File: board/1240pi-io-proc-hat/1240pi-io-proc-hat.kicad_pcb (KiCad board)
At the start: 2 copper layers, 29.2 x 58.4 mm, 7 parts, among them J21 Header, P445 Header, U445 Z80

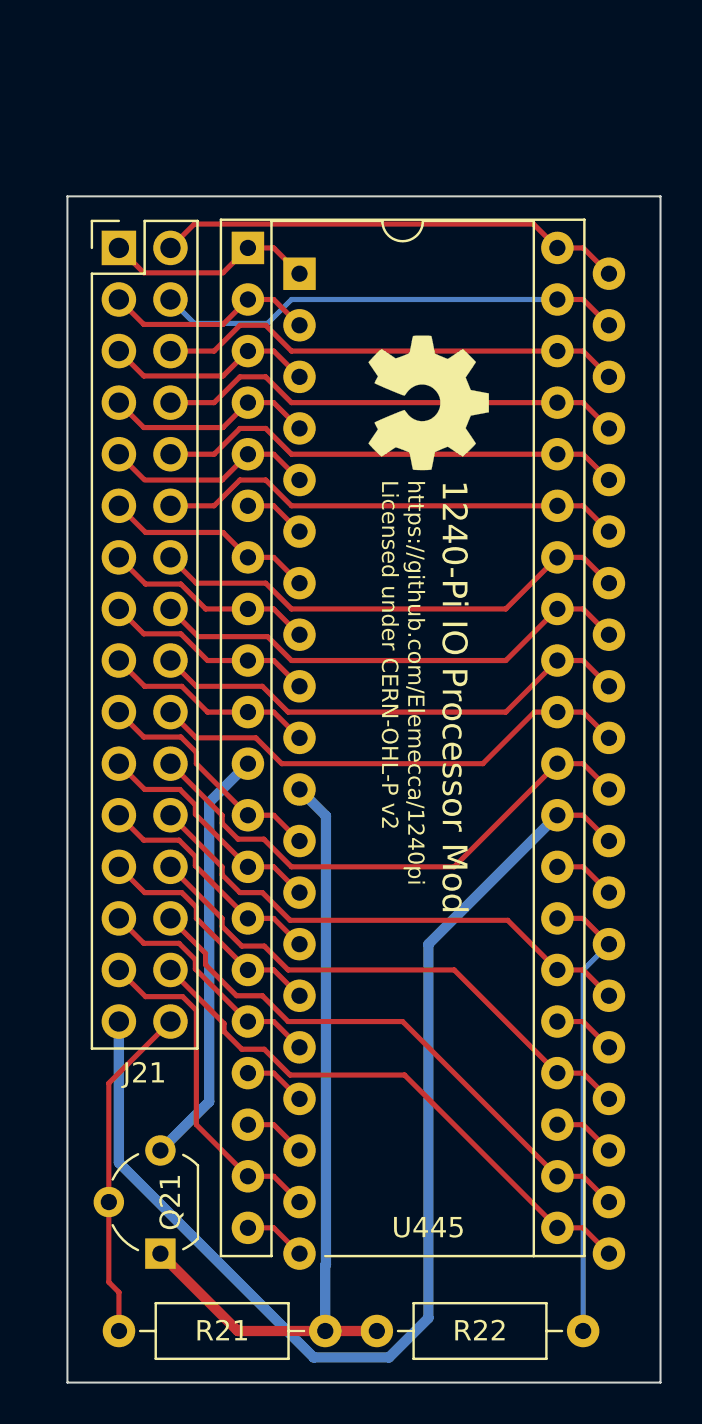
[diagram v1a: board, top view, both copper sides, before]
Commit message: Switch hat boards from IDC ribbons to flat flex cables.
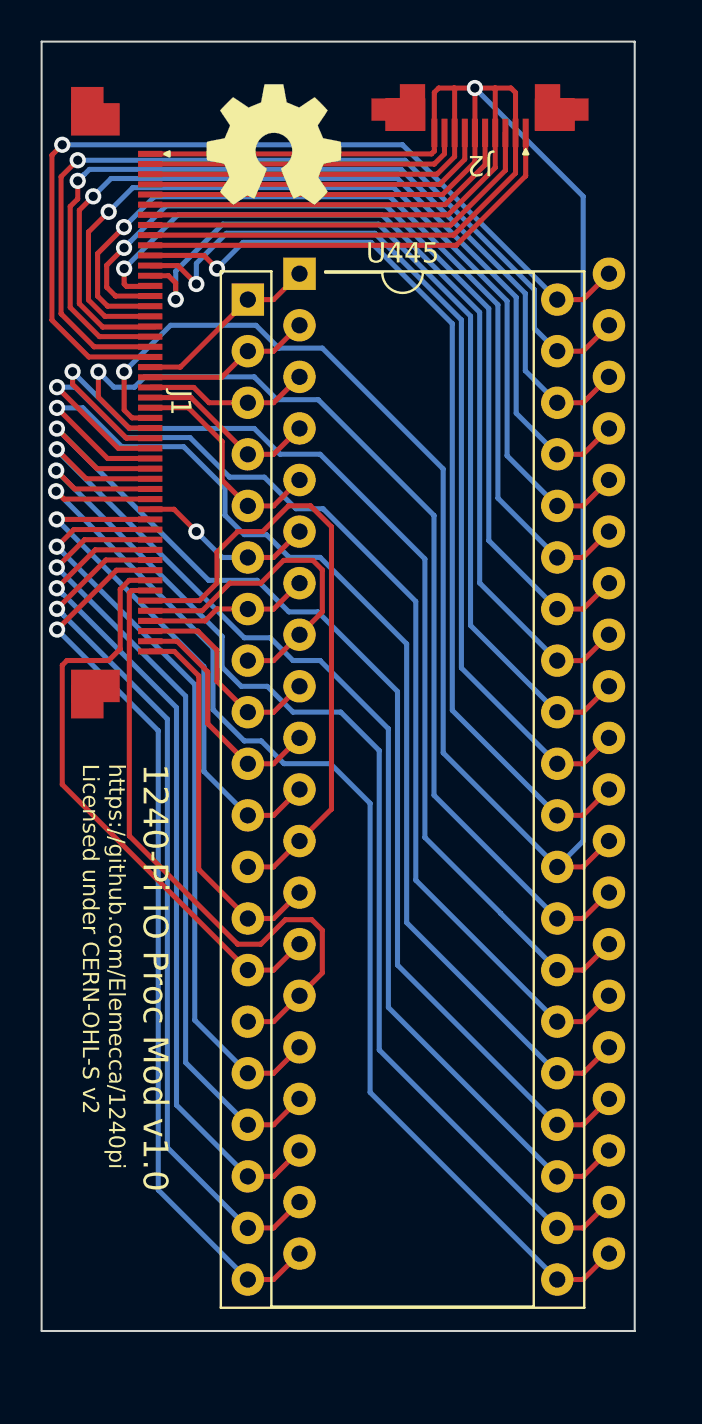
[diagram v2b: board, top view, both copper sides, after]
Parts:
- removed J21: Header, Connector_PinHeader_2.54mm:PinHeader_2x16_P2.54mm_Vertical
- removed Q21: ~, Package_TO_SOT_THT:TO-92_Wide
- removed R21, R22: 10k, Resistor_THT:R_Axial_DIN0207_L6.3mm_D2.5mm_P10.16mm_Horizontal
- added J1: 62684-50210, 0Local:Amphenol_62684-50210, F.Cu at (137.7, 58.4)
- added J2: SFV10R-1ST, 0Local:Amphenol_SFV10R-1ST, F.Cu at (156.2, 43.4)
- moved REF** 14.8 mm to (146.1, 45.7), turned to 0 degrees
- moved U445 2.55 mm to (144.8, 53.3)
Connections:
- U445 pad 11: Net-(Q21-Pad3) -> +5V
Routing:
- net GND: track 57.4 -> 194.3 mm, vias 0 -> 2
- net /~{BUSACK}: track 3.07 -> 55.8 mm, vias 0 -> 1
- net /~{BUSRQ}: track 3.07 -> 55.7 mm, vias 0 -> 1
- net /~{RFSH}: track 3.07 -> 49.8 mm, vias 0 -> 1
- net /~{IORQ}: track 3.07 -> 44.8 mm, vias 0 -> 1
- net /~{HALT}: track 3.07 -> 41.3 mm, vias 0 -> 1
- net /~{NMI}: track 3.07 -> 39.6 mm, vias 0 -> 1
- net /~{RD}: track 27.6 -> 58.7 mm, vias 0 -> 1
- net /~{M1}: track 22.6 -> 52.7 mm, vias 0 -> 1
- net /~{WR}: track 27.7 -> 57.7 mm, vias 0 -> 1
- net /~{RESET}: track 25.5 -> 54.5 mm, vias 0 -> 1
- net /~{WAIT}: track 26.6 -> 55.2 mm, vias 0 -> 1
- net /~{MREQ}: track 16.9 -> 43.0 mm, vias 0 -> 1
- net /~{INT}: track 11.8 -> 37.9 mm, vias 0 -> 1
- net /~{EXT_EN}: track 0.00 -> 22.0 mm
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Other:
- board size 29.2 x 58.4 mm -> 29.2 x 63.5 mm
- board text added: "1240-Pi IO Proc Mod v${REVISION}"
- board text added: "https://github.com/Elemecca/1240pi Licensed under CERN-OHL-S v2"
- board text removed: "1240-Pi IO Processor Mod"
- board text removed: "https://github.com/Elemecca/1240pi Licensed under CERN-OHL-P v2"

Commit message: Update board license to CERN-OHL-S v2+.
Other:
- board text added: "https://github.com/Elemecca/1240pi Licensed under CERN-OHL-S v2+"
- board text removed: "https://github.com/Elemecca/1240pi Licensed under CERN-OHL-S v2"
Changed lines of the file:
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@@
     (date "2022-05-21")
     (rev "1.0")
-    (company "© 2022 Sam Hanes, licensed under CERN-OHL-S v2")
+    (company "© 2022 Sam Hanes, licensed under CERN-OHL-S v2+")
     (comment 1 "https://github.com/Elemecca/1240pi")
-    (comment 4 "AISLER Project ID: UZHORLNP")
   )
   (layers
@@
     (effects (font (size 1.2192 1.2192) (thickness 0.2032)) (justify left))
   )
-  (gr_text "https://github.com/Elemecca/1240pi\nLicensed under CERN-OHL-S v2" (at 137.668 76.2 -90) (layer "F.SilkS")
+  (gr_text "https://github.com/Elemecca/1240pi\nLicensed under CERN-OHL-S v2+" (at 137.668 76.2 -90) (layer "F.SilkS")
     (effects (font (size 0.8 0.8) (thickness 0.1)) (justify left))
   )

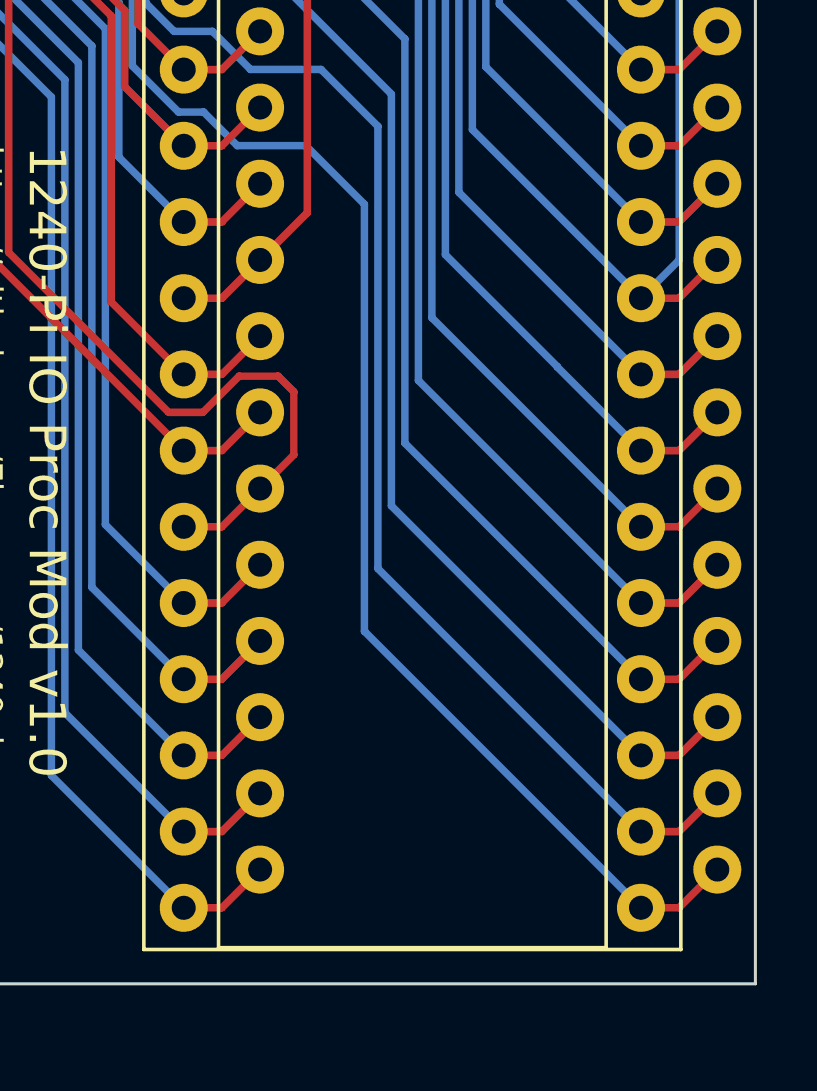
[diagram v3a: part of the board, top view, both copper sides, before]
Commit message: Disconnect and pull up Z80 pins not used by the 1240.
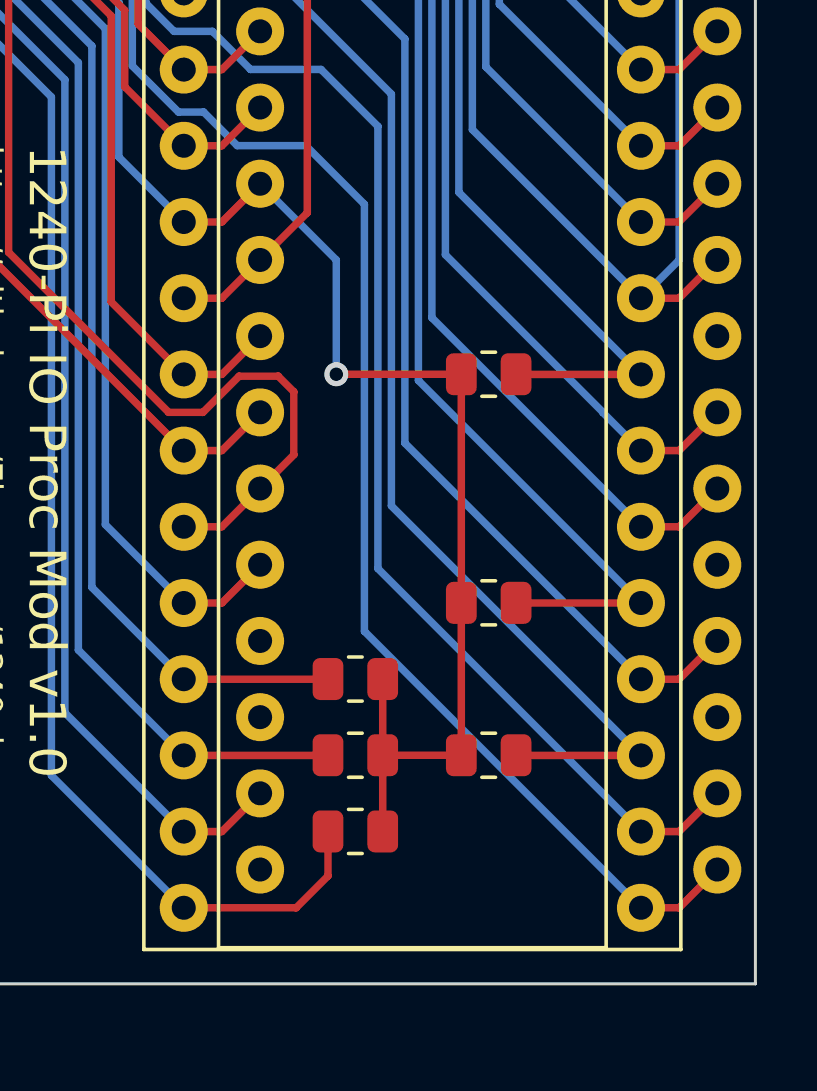
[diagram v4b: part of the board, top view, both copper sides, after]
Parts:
- added R1: 10k, Resistor_SMD:R_0805_2012Metric, F.Cu at (150.5, 94.0)
- added R2: 10k, Resistor_SMD:R_0805_2012Metric, F.Cu at (154.9, 83.8)
- added R3: 10k, Resistor_SMD:R_0805_2012Metric, F.Cu at (150.5, 96.5)
- added R4: 10k, Resistor_SMD:R_0805_2012Metric, F.Cu at (150.5, 99.1)
- added R5: 10k, Resistor_SMD:R_0805_2012Metric, F.Cu at (154.9, 91.4)
- added R6: 10k, Resistor_SMD:R_0805_2012Metric, F.Cu at (154.9, 96.5)
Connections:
- P445 pad 17: /~{NMI} -> unconnected-(P445-Pad17)
- P445 pad 18: /~{HALT} -> unconnected-(P445-Pad18)
- P445 pad 20: /~{IORQ} -> unconnected-(P445-Pad20)
- P445 pad 23: /~{BUSACK} -> unconnected-(P445-Pad23)
- P445 pad 25: /~{BUSRQ} -> unconnected-(P445-Pad25)
- P445 pad 28: /~{RFSH} -> unconnected-(P445-Pad28)
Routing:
- net +5V: track 26.2 -> 58.1 mm, vias 1 -> 2
- net /~{IORQ}: track 44.8 -> 48.4 mm
- net /~{HALT}: track 41.3 -> 43.1 mm
- net /~{NMI}: track 39.6 -> 41.3 mm
- net /~{RFSH}: track 49.8 -> 50.8 mm
- net /~{BUSRQ}: track 55.7 -> 56.8 mm
- net /~{BUSACK}: track 55.8 -> 56.9 mm

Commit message: Add bonsai logo to boards.
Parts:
- added G***: LOGO, 0Local:Symbol_Bonsai_6.7mm, F.Cu at (143.5, 44.5)
- moved REF** 3.25 mm to (148.6, 47.8)

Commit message: Export boards for manufacturing.
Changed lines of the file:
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@@
       (outputformat 1)
       (mirror false)
-      (drillshape 1)
+      (drillshape 0)
       (scaleselection 1)
-      (outputdirectory "")
+      (outputdirectory "${KIPRJMOD}/dist")
     )
   )
@@
     (fp_line (start -1 0.625) (end -1 -0.625) (layer "F.Fab") (width 0.1))
     (fp_line (start 1 0.625) (end -1 0.625) (layer "F.Fab") (width 0.1))
-    (pad "1" smd roundrect (at -0.9125 0) (size 1.025 1.4) (layers "F.Cu" "F.Paste" "F.Mask") (roundrect_rratio 0.243902)
+    (pad "1" smd roundrect (at -0.9125 0) (size 1.025 1.4) (layers "F.Cu" "F.Paste" "F.Mask") (roundrect_rratio 0.243902439)
       (net 37 "/~{IORQ}") (pintype "passive"))
-    (pad "2" smd roundrect (at 0.9125 0) (size 1.025 1.4) (layers "F.Cu" "F.Paste" "F.Mask") (roundrect_rratio 0.243902)
+    (pad "2" smd roundrect (at 0.9125 0) (size 1.025 1.4) (layers "F.Cu" "F.Paste" "F.Mask") (roundrect_rratio 0.243902439)
       (net 2 "+5V") (pintype "passive"))
     (model "${KICAD6_3DMODEL_DIR}/Resistor_SMD.3dshapes/R_0805_2012Metric.wrl"
@@
     (fp_line (start 1 -0.625) (end 1 0.625) (layer "F.Fab") (width 0.1))
     (fp_line (start 1 0.625) (end -1 0.625) (layer "F.Fab") (width 0.1))
-    (pad "1" smd roundrect (at -0.9125 0 180) (size 1.025 1.4) (layers "F.Cu" "F.Paste" "F.Mask") (roundrect_rratio 0.243902)
+    (pad "1" smd roundrect (at -0.9125 0 180) (size 1.025 1.4) (layers "F.Cu" "F.Paste" "F.Mask") (roundrect_rratio 0.243902439)
       (net 39 "/~{BUSRQ}") (pintype "passive"))
-    (pad "2" smd roundrect (at 0.9125 0 180) (size 1.025 1.4) (layers "F.Cu" "F.Paste" "F.Mask") (roundrect_rratio 0.243902)
+    (pad "2" smd roundrect (at 0.9125 0 180) (size 1.025 1.4) (layers "F.Cu" "F.Paste" "F.Mask") (roundrect_rratio 0.243902439)
       (net 2 "+5V") (pintype "passive"))
     (model "${KICAD6_3DMODEL_DIR}/Resistor_SMD.3dshapes/R_0805_2012Metric.wrl"
@@
     (fp_line (start 1 -0.625) (end 1 0.625) (layer "F.Fab") (width 0.1))
     (fp_line (start 1 0.625) (end -1 0.625) (layer "F.Fab") (width 0.1))
-    (pad "1" smd roundrect (at -0.9125 0) (size 1.025 1.4) (layers "F.Cu" "F.Paste" "F.Mask") (roundrect_rratio 0.243902)
+    (pad "1" smd roundrect (at -0.9125 0) (size 1.025 1.4) (layers "F.Cu" "F.Paste" "F.Mask") (roundrect_rratio 0.243902439)
       (net 35 "/~{NMI}") (pintype "passive"))
-    (pad "2" smd roundrect (at 0.9125 0) (size 1.025 1.4) (layers "F.Cu" "F.Paste" "F.Mask") (roundrect_rratio 0.243902)
+    (pad "2" smd roundrect (at 0.9125 0) (size 1.025 1.4) (layers "F.Cu" "F.Paste" "F.Mask") (roundrect_rratio 0.243902439)
       (net 2 "+5V") (pintype "passive"))
     (model "${KICAD6_3DMODEL_DIR}/Resistor_SMD.3dshapes/R_0805_2012Metric.wrl"
@@
     (fp_line (start 1 0.625) (end -1 0.625) (layer "F.Fab") (width 0.1))
     (fp_line (start -1 0.625) (end -1 -0.625) (layer "F.Fab") (width 0.1))
-    (pad "1" smd roundrect (at -0.9125 0) (size 1.025 1.4) (layers "F.Cu" "F.Paste" "F.Mask") (roundrect_rratio 0.243902)
+    (pad "1" smd roundrect (at -0.9125 0) (size 1.025 1.4) (layers "F.Cu" "F.Paste" "F.Mask") (roundrect_rratio 0.243902439)
       (net 36 "/~{HALT}") (pintype "passive"))
-    (pad "2" smd roundrect (at 0.9125 0) (size 1.025 1.4) (layers "F.Cu" "F.Paste" "F.Mask") (roundrect_rratio 0.243902)
+    (pad "2" smd roundrect (at 0.9125 0) (size 1.025 1.4) (layers "F.Cu" "F.Paste" "F.Mask") (roundrect_rratio 0.243902439)
       (net 2 "+5V") (pintype "passive"))
     (model "${KICAD6_3DMODEL_DIR}/Resistor_SMD.3dshapes/R_0805_2012Metric.wrl"
@@
     (fp_line (start -1 -0.625) (end 1 -0.625) (layer "F.Fab") (width 0.1))
     (fp_line (start 1 0.625) (end -1 0.625) (layer "F.Fab") (width 0.1))
-    (pad "1" smd roundrect (at -0.9125 0 180) (size 1.025 1.4) (layers "F.Cu" "F.Paste" "F.Mask") (roundrect_rratio 0.243902)
+    (pad "1" smd roundrect (at -0.9125 0 180) (size 1.025 1.4) (layers "F.Cu" "F.Paste" "F.Mask") (roundrect_rratio 0.243902439)
       (net 38 "/~{BUSACK}") (pintype "passive"))
-    (pad "2" smd roundrect (at 0.9125 0 180) (size 1.025 1.4) (layers "F.Cu" "F.Paste" "F.Mask") (roundrect_rratio 0.243902)
+    (pad "2" smd roundrect (at 0.9125 0 180) (size 1.025 1.4) (layers "F.Cu" "F.Paste" "F.Mask") (roundrect_rratio 0.243902439)
       (net 2 "+5V") (pintype "passive"))
     (model "${KICAD6_3DMODEL_DIR}/Resistor_SMD.3dshapes/R_0805_2012Metric.wrl"
@@
     (fp_line (start -1 -0.625) (end 1 -0.625) (layer "F.Fab") (width 0.1))
     (fp_line (start 1 -0.625) (end 1 0.625) (layer "F.Fab") (width 0.1))
-    (pad "1" smd roundrect (at -0.9125 0 180) (size 1.025 1.4) (layers "F.Cu" "F.Paste" "F.Mask") (roundrect_rratio 0.243902)
+    (pad "1" smd roundrect (at -0.9125 0 180) (size 1.025 1.4) (layers "F.Cu" "F.Paste" "F.Mask") (roundrect_rratio 0.243902439)
       (net 41 "/~{RFSH}") (pintype "passive"))
-    (pad "2" smd roundrect (at 0.9125 0 180) (size 1.025 1.4) (layers "F.Cu" "F.Paste" "F.Mask") (roundrect_rratio 0.243902)
+    (pad "2" smd roundrect (at 0.9125 0 180) (size 1.025 1.4) (layers "F.Cu" "F.Paste" "F.Mask") (roundrect_rratio 0.243902439)
       (net 2 "+5V") (pintype "passive"))
     (model "${KICAD6_3DMODEL_DIR}/Resistor_SMD.3dshapes/R_0805_2012Metric.wrl"

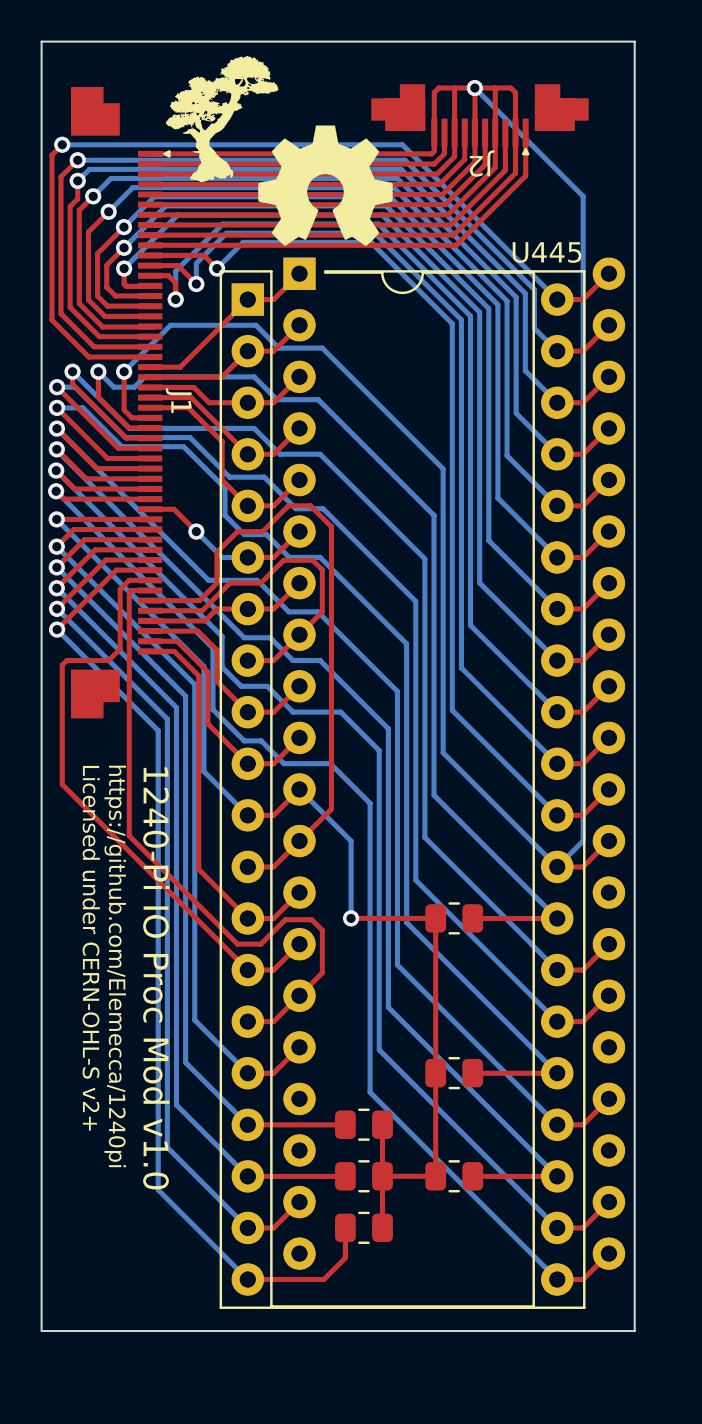
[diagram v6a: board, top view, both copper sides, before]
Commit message: Rotate sockets on hat boards 180 to match actual orientation.
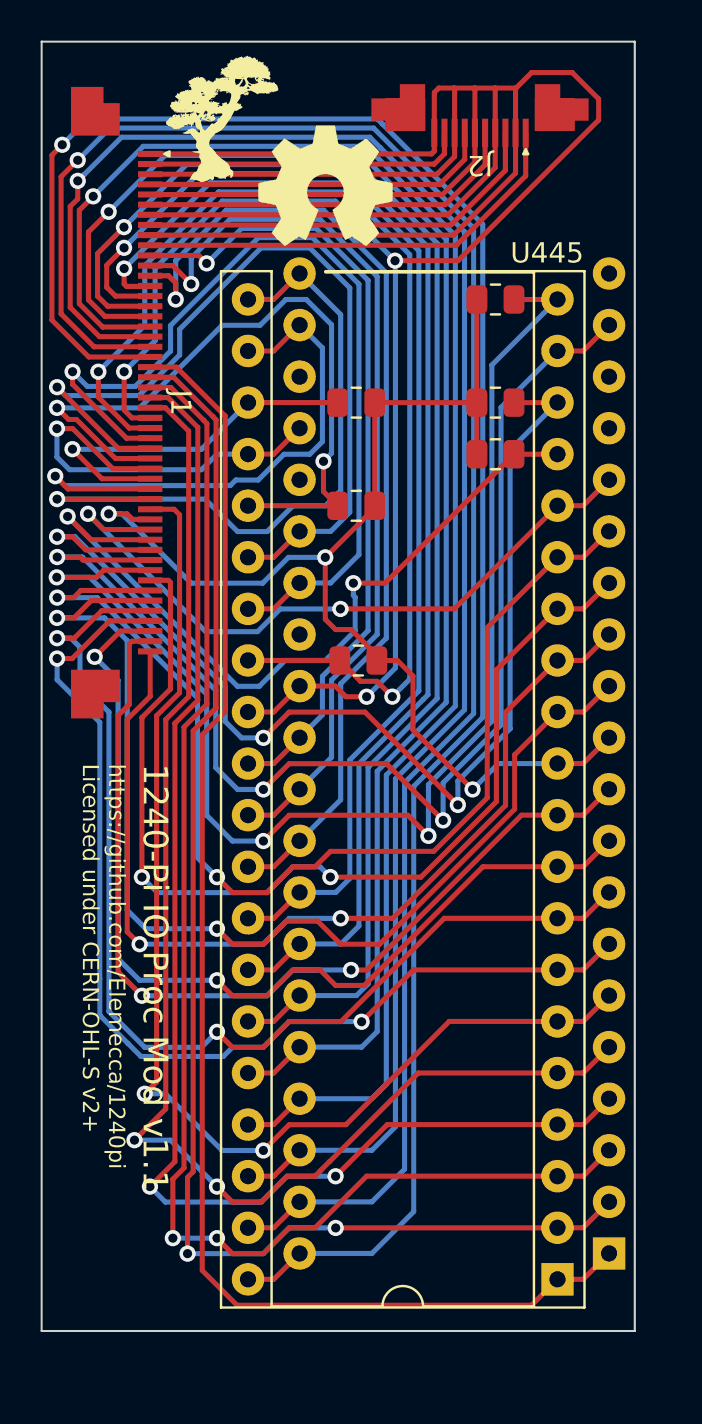
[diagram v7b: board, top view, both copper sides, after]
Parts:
- moved U445 50.6 mm to (160.0, 101.6), turned to 180 degrees
- moved P445 50.6 mm to (162.6, 100.3), turned to 180 degrees
- moved R4 46.2 mm to (157.0, 53.3), turned to 180 degrees
- moved R3 38.6 mm to (157.0, 58.4), turned to 180 degrees
- moved R6 38.4 mm to (150.1, 58.4), turned to 0 degrees
- moved R1 33.6 mm to (157.0, 61.0), turned to 180 degrees
- moved R5 28.4 mm to (150.1, 63.5), turned to 0 degrees
- moved R2 13.5 mm to (150.2, 71.1), turned to 0 degrees
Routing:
- net /A13: track 8.19 -> 68.3 mm, vias 0 -> 2
- net /A11: track 9.26 -> 69.0 mm
- net /A12: track 8.41 -> 67.6 mm, vias 0 -> 2
- net /A14: track 9.04 -> 66.4 mm, vias 0 -> 2
- net /A15: track 11.0 -> 66.2 mm, vias 0 -> 2
- net /A10: track 45.0 -> 97.4 mm
- net /~{CLK}: track 8.86 -> 58.0 mm, vias 1 -> 2
- net /A9: track 44.7 -> 91.8 mm
- net /D4: track 8.13 -> 52.0 mm, vias 0 -> 2
- net /A8: track 44.8 -> 86.5 mm
- net /~{BUSACK}: track 56.9 -> 18.5 mm
- net /D3: track 16.4 -> 54.1 mm, vias 0 -> 2
- net /D5: track 10.4 -> 47.3 mm, vias 0 -> 2
- net /A7: track 45.0 -> 81.3 mm
- net /~{WAIT}: track 55.2 -> 19.9 mm
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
